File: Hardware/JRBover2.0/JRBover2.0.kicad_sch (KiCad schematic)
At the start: 25 parts, among them J10 Input of Driver L9110, J2 HC_SRO4, J3 HC_SRO4, J4 HC_SRO4, J5 CableAlimentacion, J6 SWITCH, J7 Programador, J8 BOTON, U1 ESP32-WROOM-32, U2 L7805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

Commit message: en correcion por bustos, ya casi
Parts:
- C2, C4, C5, C6: footprint (none) -> Capacitor_SMD:C_1206_3216Metric
- J1: value (none) -> EncoderMotorDerecha
- J9: value (none) -> EncoderMotorIzquierda
- LED1, LED2: footprint (none) -> LED_SMD:LED_1206_3216Metric
- R1, R2: footprint (none) -> EESTN5:R_1206
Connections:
- net OUT_IR1 is gone; now on net D0: U1.14 (IO12)
- net D0: no longer U1.13 (IO14)
- net IN3: now also U1.36 (IO22); no longer U1.29 (IO5)
- net IN4: now also U1.37 (IO23); no longer U1.30 (IO18)
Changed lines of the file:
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@@
     (stroke (width 0) (type default) (color 0 0 0 0))
   )
+  (wire (pts (xy 158.8262 77.724) (xy 163.3982 77.724))
+    (stroke (width 0) (type default) (color 0 0 0 0))
+  )
   (wire (pts (xy 163.3982 44.704) (xy 158.8262 44.704))
     (stroke (width 0) (type default) (color 0 0 0 0))
@@
     (stroke (width 0) (type default) (color 0 0 0 0))
   )
+  (wire (pts (xy 158.8262 75.184) (xy 163.3982 75.184))
+    (stroke (width 0) (type default) (color 0 0 0 0))
+  )
   (wire (pts (xy 39.5732 82.7532) (xy 41.91 82.7532))
     (stroke (width 0) (type default) (color 0 0 0 0))
@@
     (stroke (width 0) (type default) (color 0 0 0 0))
   )
-  (wire (pts (xy 158.8262 67.564) (xy 163.3982 67.564))
-    (stroke (width 0) (type default) (color 0 0 0 0))
-  )
   (wire (pts (xy 85.4202 81.915) (xy 88.2396 81.915))
     (stroke (width 0) (type default) (color 0 0 0 0))
@@
     (stroke (width 0) (type default) (color 0 0 0 0))
   )
-  (wire (pts (xy 158.8262 49.784) (xy 163.3982 49.784))
-    (stroke (width 0) (type default) (color 0 0 0 0))
-  )
   (wire (pts (xy 78.1812 26.035) (xy 76.2508 26.035))
     (stroke (width 0) (type default) (color 0 0 0 0))
@@
     (stroke (width 0) (type default) (color 0 0 0 0))
   )
-  (wire (pts (xy 158.8262 52.324) (xy 163.2966 52.324))
-    (stroke (width 0) (type default) (color 0 0 0 0))
-  )
   (wire (pts (xy 88.265 109.22) (xy 88.265 109.855))
     (stroke (width 0) (type default) (color 0 0 0 0))
@@
     (stroke (width 0) (type default) (color 0 0 0 0))
   )
-  (wire (pts (xy 158.8262 57.404) (xy 165.9382 57.404))
+  (wire (pts (xy 158.8262 52.324) (xy 165.9382 52.324))
     (stroke (width 0) (type default) (color 0 0 0 0))
   )
@@
     (effects (font (size 1.27 1.27)) (justify left bottom))
   )
-  (label "Trig1" (at 164.0332 87.884 0)
+  (label "D0" (at 165.9382 52.324 180)
+    (effects (font (size 1.27 1.27)) (justify right bottom))
+  )
+  (label "IN3" (at 163.3982 75.184 0)
     (effects (font (size 1.27 1.27)) (justify left bottom))
   )
-  (label "IN2" (at 163.3982 47.244 0)
+  (label "Trig1" (at 164.0332 87.884 0)
     (effects (font (size 1.27 1.27)) (justify left bottom))
   )
-  (label "IN3" (at 163.3982 49.784 0)
+  (label "IN2" (at 163.3982 47.244 0)
     (effects (font (size 1.27 1.27)) (justify left bottom))
   )
@@
     (effects (font (size 1.27 1.27)) (justify right bottom))
   )
-  (label "D0" (at 165.9382 57.404 180)
-    (effects (font (size 1.27 1.27)) (justify right bottom))
-  )
   (label "IN1" (at 254.0508 48.7172 180)
     (effects (font (size 1.27 1.27)) (justify right bottom))
@@
     (effects (font (size 1.27 1.27)) (justify left bottom))
   )
-  (label "IN4" (at 163.3982 67.564 0)
-    (effects (font (size 1.27 1.27)) (justify left bottom))
-  )
   (label "Trig2" (at 165.1762 90.424 0)
     (effects (font (size 1.27 1.27)) (justify left bottom))
@@
     (effects (font (size 1.27 1.27)) (justify left bottom))
   )
-  (label "OUT_IR1" (at 163.2966 52.324 0)
-    (effects (font (size 1.27 1.27)) (justify left bottom))
-  )
   (label "Echo3" (at 163.2712 85.3186 0)
     (effects (font (size 1.27 1.27)) (justify left bottom))
@@
     (effects (font (size 1.27 1.27)) (justify right bottom))
   )
+  (label "IN4" (at 163.3982 77.724 0)
+    (effects (font (size 1.27 1.27)) (justify left bottom))
+  )
   (label "Echo2" (at 43.0022 52.324 0)
     (effects (font (size 1.27 1.27)) (justify left bottom))
@@
       (effects (font (size 1.27 1.27)) (justify left))
     )
-    (property "Footprint" "" (id 2) (at 111.0742 44.704 0)
+    (property "Footprint" "Capacitor_SMD:C_1206_3216Metric" (id 2) (at 111.0742 44.704 0)
       (effects (font (size 1.27 1.27)) hide)
     )
@@
       (effects (font (size 1.27 1.27)) (justify right))
     )
-    (property "Footprint" "" (id 2) (at 215.5952 39.243 0)
+    (property "Footprint" "Capacitor_SMD:C_1206_3216Metric" (id 2) (at 215.5952 39.243 0)
       (effects (font (size 1.27 1.27)) hide)
     )
@@
       (effects (font (size 1.016 1.016)) (justify left))
     )
-    (property "Footprint" "" (id 2) (at 224.8662 38.862 0)
+    (property "Footprint" "LED_SMD:LED_1206_3216Metric" (id 2) (at 224.8662 38.862 0)
       (effects (font (size 1.524 1.524)) hide)
     )
@@
       (effects (font (size 1.27 1.27)) (justify left))
     )
-    (property "Value" "" (id 1) (at 261.112 85.1412 0)
+    (property "Value" "EncoderMotorDerecha" (id 1) (at 261.112 85.1412 0)
       (effects (font (size 1.27 1.27)) (justify left))
     )
@@
       (effects (font (size 1.016 1.016)))
     )
-    (property "Footprint" "" (id 2) (at 217.7542 93.472 0)
+    (property "Footprint" "LED_SMD:LED_1206_3216Metric" (id 2) (at 217.7542 93.472 0)
       (effects (font (size 1.524 1.524)) hide)
     )
@@
       (effects (font (size 1.27 1.27)) (justify left))
     )
-    (property "Footprint" "" (id 2) (at 188.0362 40.259 0)
+    (property "Footprint" "Capacitor_SMD:C_1206_3216Metric" (id 2) (at 188.0362 40.259 0)
       (effects (font (size 1.27 1.27)) hide)
     )
@@
       (effects (font (size 1.27 1.27)) (justify right))
     )
-    (property "Footprint" "" (id 2) (at 222.9612 84.963 90)
+    (property "Footprint" "EESTN5:R_1206" (id 2) (at 222.9612 84.963 90)
       (effects (font (size 1.27 1.27)) hide)
     )
@@
       (effects (font (size 1.27 1.27)) (justify right))
     )
-    (property "Footprint" "" (id 2) (at 212.8012 87.249 0)
+    (property "Footprint" "Capacitor_SMD:C_1206_3216Metric" (id 2) (at 212.8012 87.249 0)
       (effects (font (size 1.27 1.27)) hide)
     )
@@
       (effects (font (size 1.27 1.27)) (justify left))
     )
-    (property "Value" "" (id 1) (at 261.112 100.3812 0)
+    (property "Value" "EncoderMotorIzquierda" (id 1) (at 261.112 100.3812 0)
       (effects (font (size 1.27 1.27)) (justify left))
     )
@@
     (property "Reference" "R1" (id 0) (at 221.0562 27.9232 90))
     (property "Value" "470" (id 1) (at 221.0562 30.4601 90))
-    (property "Footprint" "" (id 2) (at 221.0562 30.861 90)
+    (property "Footprint" "EESTN5:R_1206" (id 2) (at 221.0562 30.861 90)
       (effects (font (size 1.27 1.27)) hide)
     )

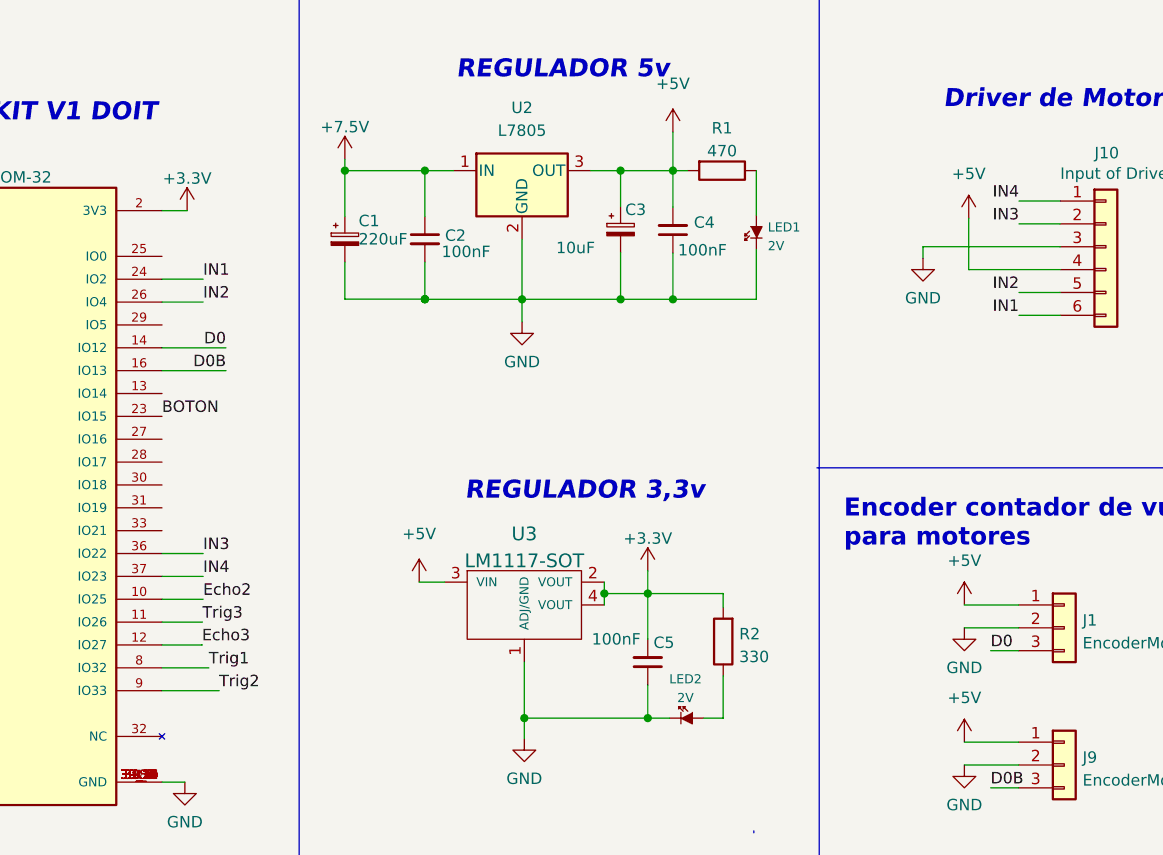
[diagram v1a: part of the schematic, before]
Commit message: el anterior tenia erro de antena esp32 , esta vez esta en la orilla espera correccion:)
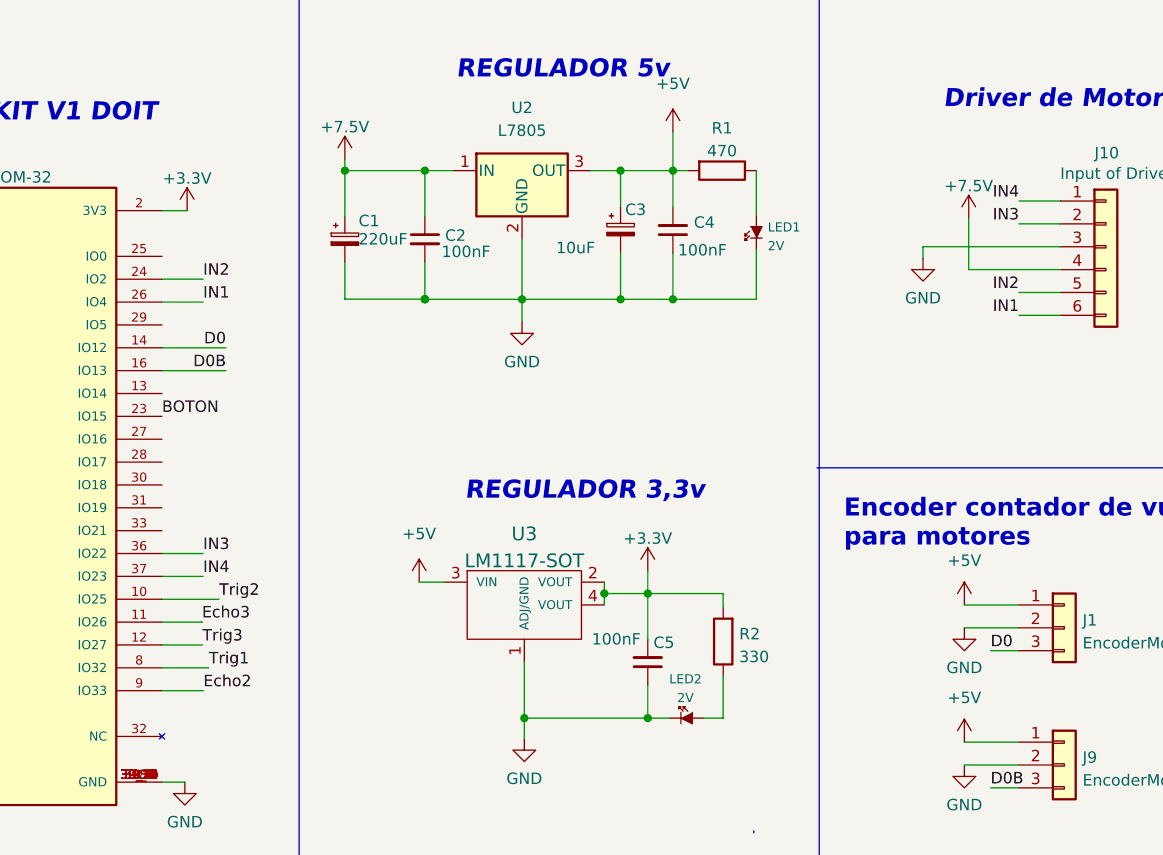
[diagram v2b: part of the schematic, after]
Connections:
- net +5V: no longer J10.4 (Pin_4)
- net +7.5V: now also J10.4 (Pin_4)
- net Echo2: now also U1.9 (IO33); no longer U1.10 (IO25)
- net Echo3: now also U1.11 (IO26); no longer U1.12 (IO27)
- net IN1: now also U1.26 (IO4); no longer U1.24 (IO2)
- net IN2: now also U1.24 (IO2); no longer U1.26 (IO4)
- net Trig2: now also U1.10 (IO25); no longer U1.9 (IO33)
- net Trig3: now also U1.12 (IO27); no longer U1.11 (IO26)
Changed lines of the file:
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@@
     (stroke (width 0) (type default) (color 0 0 0 0))
   )
-  (wire (pts (xy 158.8262 90.424) (xy 165.1762 90.424))
+  (wire (pts (xy 179.1462 42.799) (xy 179.1462 46.9138))
     (stroke (width 0) (type default) (color 0 0 0 0))
   )
-  (wire (pts (xy 179.1462 42.799) (xy 179.1462 46.9138))
+  (wire (pts (xy 163.322 85.344) (xy 158.8262 85.344))
     (stroke (width 0) (type default) (color 0 0 0 0))
   )
@@
     (stroke (width 0) (type default) (color 0 0 0 0))
   )
+  (wire (pts (xy 158.8262 90.424) (xy 163.4236 90.424))
+    (stroke (width 0) (type default) (color 0 0 0 0))
+  )
   (wire (pts (xy 88.265 106.68) (xy 88.265 106.045))
     (stroke (width 0) (type default) (color 0 0 0 0))
@@
     (stroke (width 0) (type default) (color 0 0 0 0))
   )
-  (wire (pts (xy 163.322 82.804) (xy 158.8262 82.804))
-    (stroke (width 0) (type default) (color 0 0 0 0))
-  )
   (wire (pts (xy 39.0906 30.988) (xy 42.6466 30.988))
     (stroke (width 0) (type default) (color 0 0 0 0))
@@
     (stroke (width 0) (type default) (color 0 0 0 0))
   )
-  (wire (pts (xy 163.3982 44.704) (xy 158.8262 44.704))
-    (stroke (width 0) (type default) (color 0 0 0 0))
-  )
   (wire (pts (xy 158.8262 37.084) (xy 161.6202 37.084))
     (stroke (width 0) (type default) (color 0 0 0 0))
@@
     (stroke (width 0) (type default) (color 0 0 0 0))
   )
+  (wire (pts (xy 158.8262 82.804) (xy 163.2712 82.804))
+    (stroke (width 0) (type default) (color 0 0 0 0))
+  )
   (wire (pts (xy 258.6228 48.7172) (xy 254.0508 48.7172))
     (stroke (width 0) (type default) (color 0 0 0 0))
   )
-  (wire (pts (xy 85.4202 81.915) (xy 88.2396 81.915))
+  (wire (pts (xy 163.2712 82.7786) (xy 163.2712 82.804))
     (stroke (width 0) (type default) (color 0 0 0 0))
   )
-  (wire (pts (xy 158.8262 85.344) (xy 163.2712 85.344))
+  (wire (pts (xy 85.4202 81.915) (xy 88.2396 81.915))
     (stroke (width 0) (type default) (color 0 0 0 0))
   )
@@
     (stroke (width 0) (type default) (color 0 0 0 0))
   )
+  (wire (pts (xy 158.8262 44.704) (xy 163.3982 44.704))
+    (stroke (width 0) (type default) (color 0 0 0 0))
+  )
   (wire (pts (xy 41.783 49.784) (xy 39.37 49.784))
     (stroke (width 0) (type default) (color 0 0 0 0))
@@
     (stroke (width 0) (type default) (color 0 0 0 0))
   )
+  (wire (pts (xy 163.3982 47.244) (xy 158.8262 47.244))
+    (stroke (width 0) (type default) (color 0 0 0 0))
+  )
   (wire (pts (xy 88.265 109.22) (xy 88.265 109.855))
     (stroke (width 0) (type default) (color 0 0 0 0))
@@
     (stroke (width 0) (type default) (color 0 0 0 0))
   )
-  (wire (pts (xy 163.2712 85.3186) (xy 163.2712 85.344))
-    (stroke (width 0) (type default) (color 0 0 0 0))
-  )
   (wire (pts (xy 41.783 48.641) (xy 41.783 49.784))
     (stroke (width 0) (type default) (color 0 0 0 0))
@@
     (stroke (width 0) (type default) (color 0 0 0 0))
   )
-  (wire (pts (xy 163.3982 80.264) (xy 158.8262 80.264))
-    (stroke (width 0) (type default) (color 0 0 0 0))
-  )
   (polyline (pts (xy 105.4862 12.7) (xy 105.4862 130.81))
     (stroke (width 0) (type default) (color 0 0 0 0))
@@
     (stroke (width 0) (type default) (color 0 0 0 0))
   )
-  (wire (pts (xy 158.8262 47.244) (xy 163.3982 47.244))
-    (stroke (width 0) (type default) (color 0 0 0 0))
-  )
   (wire (pts (xy 41.5036 24.765) (xy 41.5036 25.908))
     (stroke (width 0) (type default) (color 0 0 0 0))
@@
     (stroke (width 0) (type default) (color 0 0 0 0))
   )
+  (wire (pts (xy 158.8262 80.264) (xy 165.1762 80.264))
+    (stroke (width 0) (type default) (color 0 0 0 0))
+  )
   (polyline (pts (xy 105.4862 130.81) (xy 174.0662 131.064))
     (stroke (width 0) (type default) (color 0 0 0 0))
@@
     (effects (font (size 2 2) (thickness 0.254) bold italic) (justify left bottom))
   )
-  (label "IN1" (at 163.3982 44.704 0)
-    (effects (font (size 1.27 1.27)) (justify left bottom))
-  )
   (label "Trig3" (at 43.1292 80.2132 0)
     (effects (font (size 1.27 1.27)) (justify left bottom))
@@
     (effects (font (size 1.27 1.27)) (justify left bottom))
   )
-  (label "Trig1" (at 164.0332 87.884 0)
-    (effects (font (size 1.27 1.27)) (justify left bottom))
-  )
-  (label "IN2" (at 163.3982 47.244 0)
+  (label "IN2" (at 163.3982 44.704 0)
     (effects (font (size 1.27 1.27)) (justify left bottom))
   )
@@
     (effects (font (size 1.27 1.27)) (justify left bottom))
   )
+  (label "IN1" (at 163.3982 47.244 0)
+    (effects (font (size 1.27 1.27)) (justify left bottom))
+  )
   (label "BOTON" (at 79.7052 64.77 180)
     (effects (font (size 1.27 1.27)) (justify right bottom))
@@
     (effects (font (size 1.27 1.27)) (justify left bottom))
   )
-  (label "Trig2" (at 165.1762 90.424 0)
+  (label "Trig2" (at 165.1762 80.264 0)
     (effects (font (size 1.27 1.27)) (justify left bottom))
   )
@@
     (effects (font (size 1.524 1.524)) (justify right bottom))
   )
-  (label "BOTON" (at 158.8262 59.944 0)
+  (label "Echo3" (at 163.2712 82.7786 0)
     (effects (font (size 1.27 1.27)) (justify left bottom))
   )
-  (label "D0B" (at 250.9012 101.219 0)
+  (label "BOTON" (at 158.8262 59.944 0)
     (effects (font (size 1.27 1.27)) (justify left bottom))
   )
-  (label "Echo3" (at 163.2712 85.3186 0)
+  (label "D0B" (at 250.9012 101.219 0)
     (effects (font (size 1.27 1.27)) (justify left bottom))
   )
@@
     (effects (font (size 1.27 1.27)) (justify right bottom))
   )
+  (label "Trig1" (at 164.0332 87.884 0)
+    (effects (font (size 1.27 1.27)) (justify left bottom))
+  )
+  (label "Echo2" (at 163.4236 90.424 0)
+    (effects (font (size 1.27 1.27)) (justify left bottom))
+  )
   (label "VBAT" (at 88.265 106.045 0)
     (effects (font (size 1.524 1.524)) (justify left bottom))
@@
     (effects (font (size 1.27 1.27)) (justify left bottom))
   )
+  (label "Trig3" (at 163.322 85.344 0)
+    (effects (font (size 1.27 1.27)) (justify left bottom))
+  )
   (label "D0B" (at 165.9382 54.864 180)
     (effects (font (size 1.27 1.27)) (justify right bottom))
@@
     (effects (font (size 1.27 1.27)) (justify right bottom))
   )
-  (label "Echo2" (at 163.3982 80.264 0)
-    (effects (font (size 1.27 1.27)) (justify left bottom))
-  )
   (label "Echo" (at 113.9952 57.404 180)
     (effects (font (size 1.27 1.27)) (justify right bottom))
@@
     (effects (font (size 1.27 1.27)) (justify left bottom))
   )
-  (label "Trig3" (at 163.322 82.804 0)
-    (effects (font (size 1.27 1.27)) (justify left bottom))
-  )
   (symbol (lib_id "Connector_Generic:Conn_01x04") (at 34.29 52.324 0) (mirror y) (unit 1)
     (in_bom yes) (on_board yes)
@@
     (pin "1")
   )
+  (symbol (lib_id "power:+7.5V") (at 248.4628 37.9222 0) (unit 1)
+    (in_bom yes) (on_board yes) (fields_autoplaced)
+    (property "Reference" "#PWR0106" (id 0) (at 248.4628 41.7322 0)
+      (effects (font (size 1.27 1.27)) hide)
+    )
+    (property "Value" "+7.5V" (id 1) (at 248.4628 34.3464 0))
+    (property "Footprint" "" (id 2) (at 248.4628 37.9222 0)
+      (effects (font (size 1.27 1.27)) hide)
+    )
+    (property "Datasheet" "" (id 3) (at 248.4628 37.9222 0)
+      (effects (font (size 1.27 1.27)) hide)
+    )
+    (pin "1")
+  )
   (symbol (lib_id "power:GND") (at 243.3828 42.3672 0) (unit 1)
     (in_bom yes) (on_board yes) (fields_autoplaced)
@@
     (pin "4")
   )
-  (symbol (lib_id "power:+5V") (at 248.4628 37.9222 0) (unit 1)
-    (in_bom yes) (on_board yes) (fields_autoplaced)
-    (property "Reference" "#PWR0106" (id 0) (at 248.4628 41.7322 0)
-      (effects (font (size 1.27 1.27)) hide)
-    )
-    (property "Value" "+5V" (id 1) (at 248.4628 32.9946 0))
-    (property "Footprint" "" (id 2) (at 248.4628 37.9222 0)
-      (effects (font (size 1.27 1.27)) hide)
-    )
-    (property "Datasheet" "" (id 3) (at 248.4628 37.9222 0)
-      (effects (font (size 1.27 1.27)) hide)
-    )
-    (pin "1")
-  )
   (symbol (lib_id "power:GND") (at 88.265 109.855 0) (unit 1)
     (in_bom yes) (on_board yes) (fields_autoplaced)
@@
       (reference "#PWR0105") (unit 1) (value "GND") (footprint "")
     )
-    (path "/f36e0700-1d33-47c5-b8de-76e4b6cfa9f9"
-      (reference "#PWR0106") (unit 1) (value "+5V") (footprint "")
+    (path "/a899b179-b86c-45b0-8a6e-1c7aa4ee7e73"
+      (reference "#PWR0106") (unit 1) (value "+7.5V") (footprint "")
     )
     (path "/04addc8b-f9ee-4148-9f0f-21fd85407029"
